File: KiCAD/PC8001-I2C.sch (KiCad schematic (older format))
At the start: 35 parts, among them J1 ADDR-JP, J2 I2C RTC DS3231, J3 I2C OUT, J4 PC8001 Ext Con, Q1 2N7000, U1 74HC138, U2 DS1307+, U3 8255, U4 74HC4066, U5 24LC1025, U6 24LC1025, Y1 32.768kHz

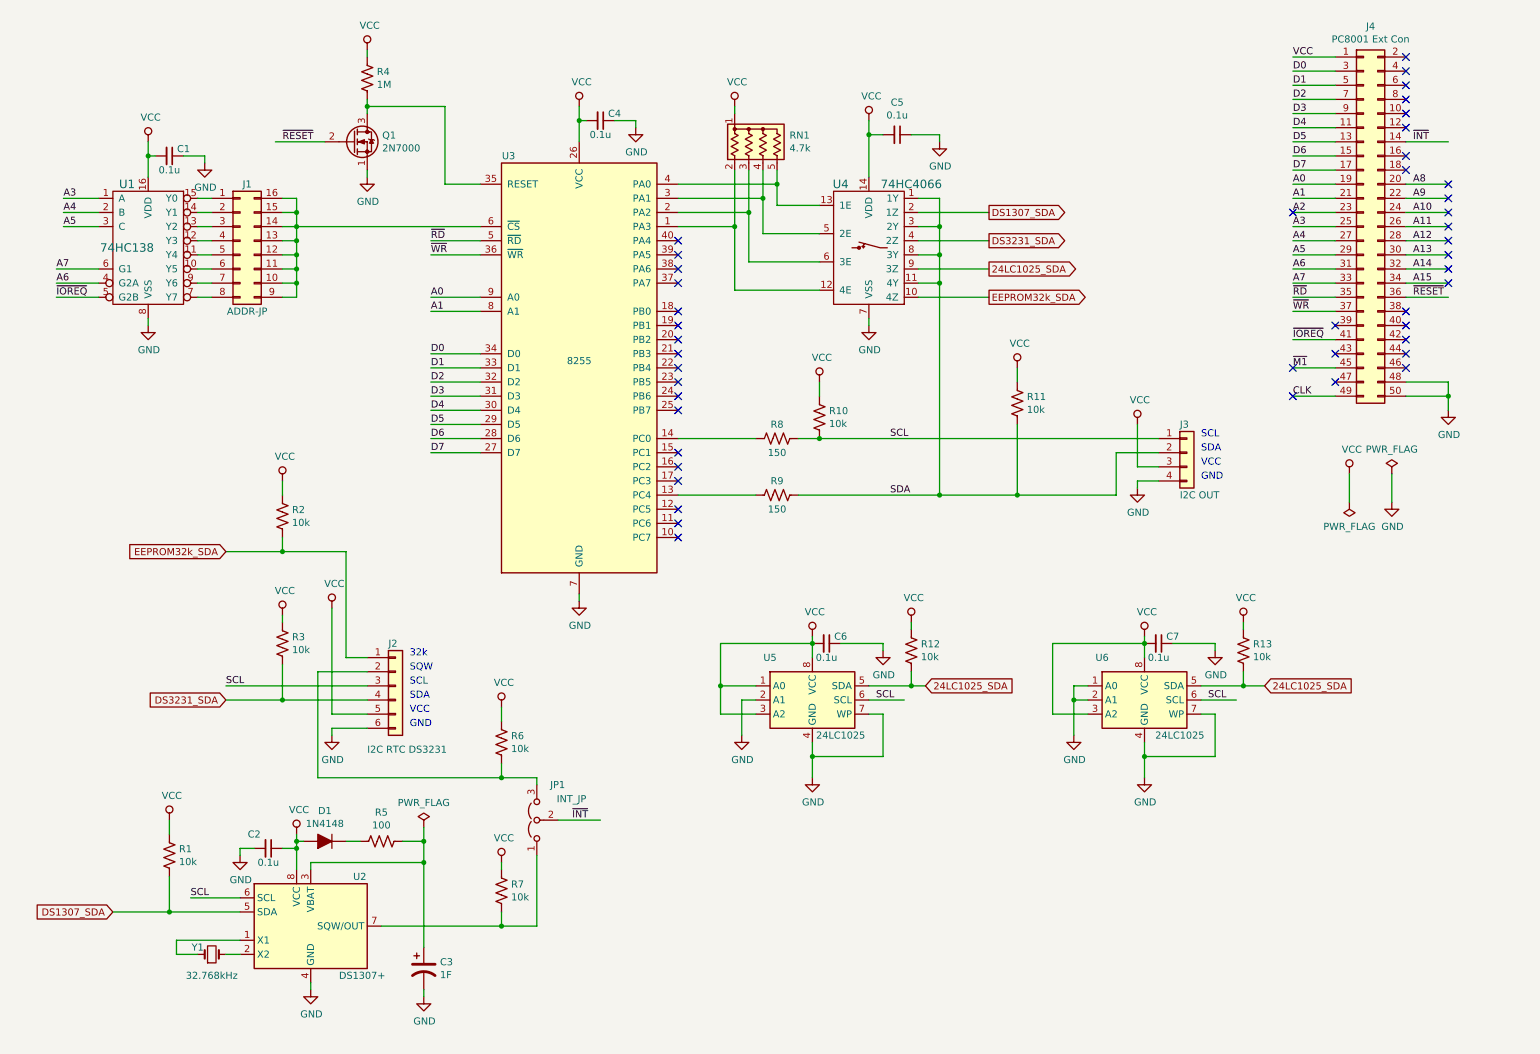
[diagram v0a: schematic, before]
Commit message: 回路変更、I2C RTC(DS3231)サンプル作成
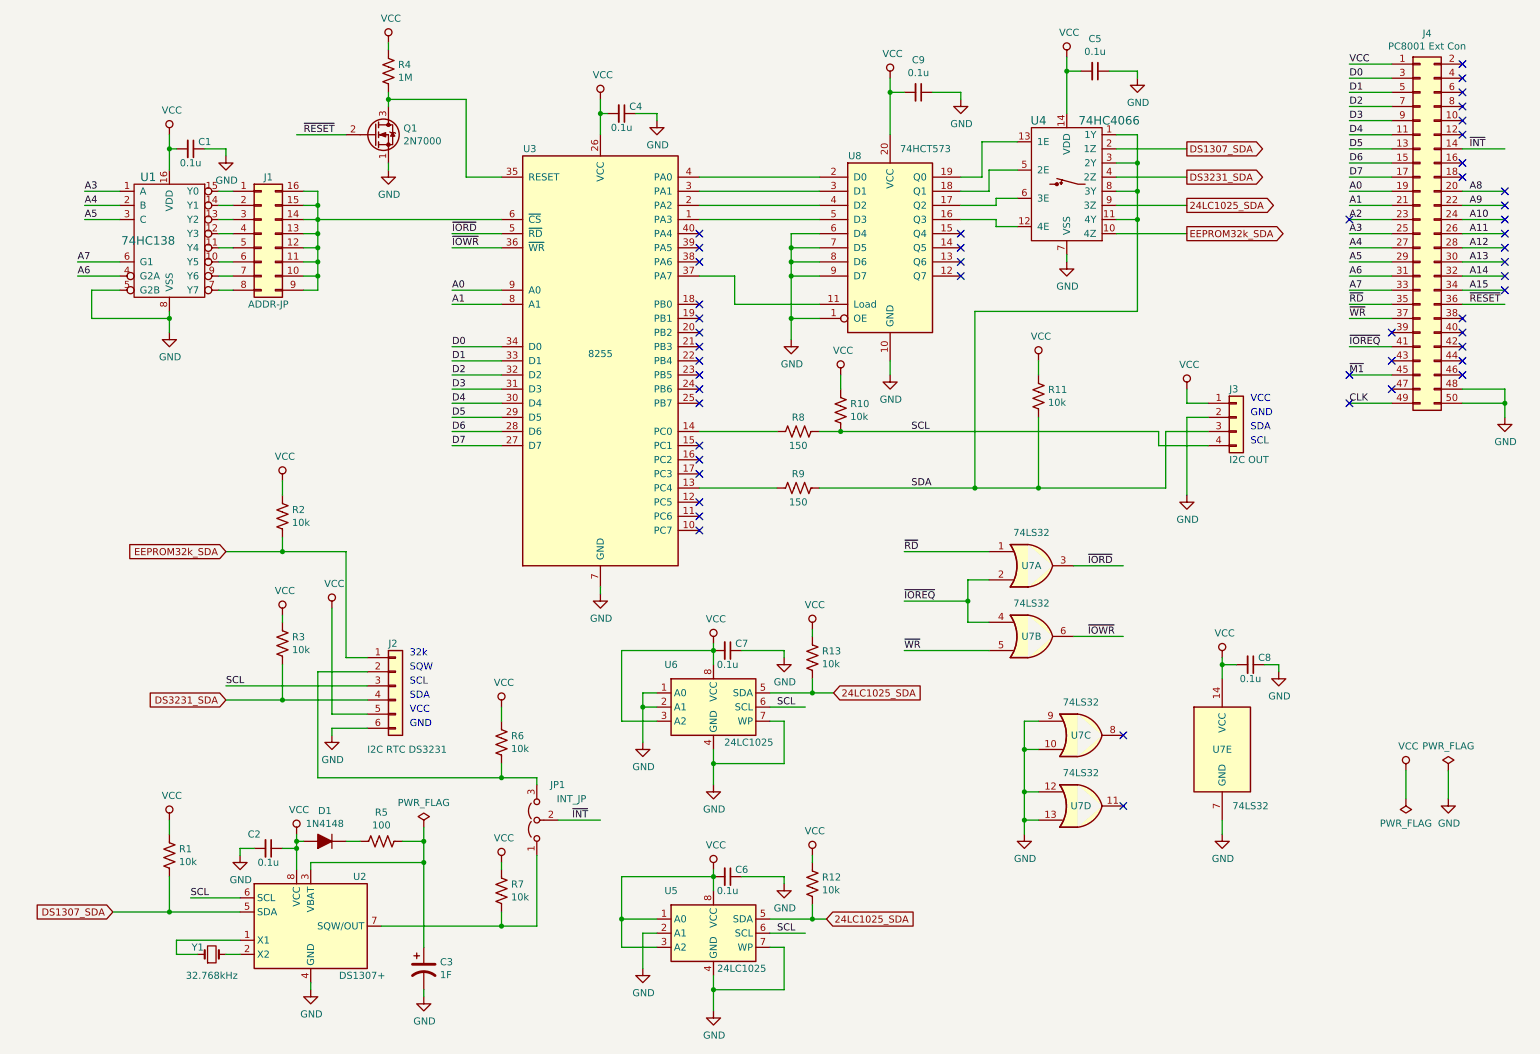
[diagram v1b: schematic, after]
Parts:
- removed RN1: 4.7k, Resistor_THT:R_Array_SIP5, symbol Device:R_Network04_US
- added C8, C9: 0.1u, symbol Device:C_Small
- added U7: 74LS32, symbol 74xx:74LS32
- added U8: 74HCT573, symbol 74xx:74LS573
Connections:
- net GND: now also J3.2 (Pin_2), U1.5 (G2B), C8.1, C9.1, U7.10, U7.12, U7.13, U7.7 (GND), U7.9, U8.1 (OE), U8.10 (GND), U8.6 (D4), U8.7 (D5), U8.8 (D6), U8.9 (D7); no longer J3.4 (Pin_4)
- net SCL: now also J3.4 (Pin_4); no longer J3.1 (Pin_1)
- net SDA: now also J3.3 (Pin_3); no longer J3.2 (Pin_2)
- net VCC: now also J3.1 (Pin_1), C8.2, C9.2, U7.14 (VCC), U8.20 (VCC); no longer J3.3 (Pin_3)
- net ~IOREQ: now also U7.2, U7.4; no longer U1.5 (G2B)
- net ~RD: now also U7.1; no longer U3.5 (~RD~)
- net ~WR: now also U7.5; no longer U3.36 (~WR~)
- net at U4.12 (4E): now also U8.16 (Q3); no longer U3.1 (PA3)
- net at U4.13 (1E): now also U8.19 (Q0); no longer U3.4 (PA0)
- net at U4.5 (2E): now also U8.18 (Q1); no longer U3.3 (PA1)
- net at U4.6 (3E): now also U8.17 (Q2); no longer U3.2 (PA2)
- net at U3.37 (PA7): now also U8.11 (Load)
- new net: U3.1 (PA3), U8.5 (D3)
- new net: U3.2 (PA2), U8.4 (D2)
- new net: U3.3 (PA1), U8.3 (D1)
- new net: U3.4 (PA0), U8.2 (D0)
- new net ~IORD: U3.5 (~RD~), U7.3
- new net ~IOWR: U3.36 (~WR~), U7.6
- no-connect marks 45 -> 50
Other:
- moved on the sheet: C1, C4, C5, C6, C7, J1, J3, J4, Q1, R10, R11, R12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

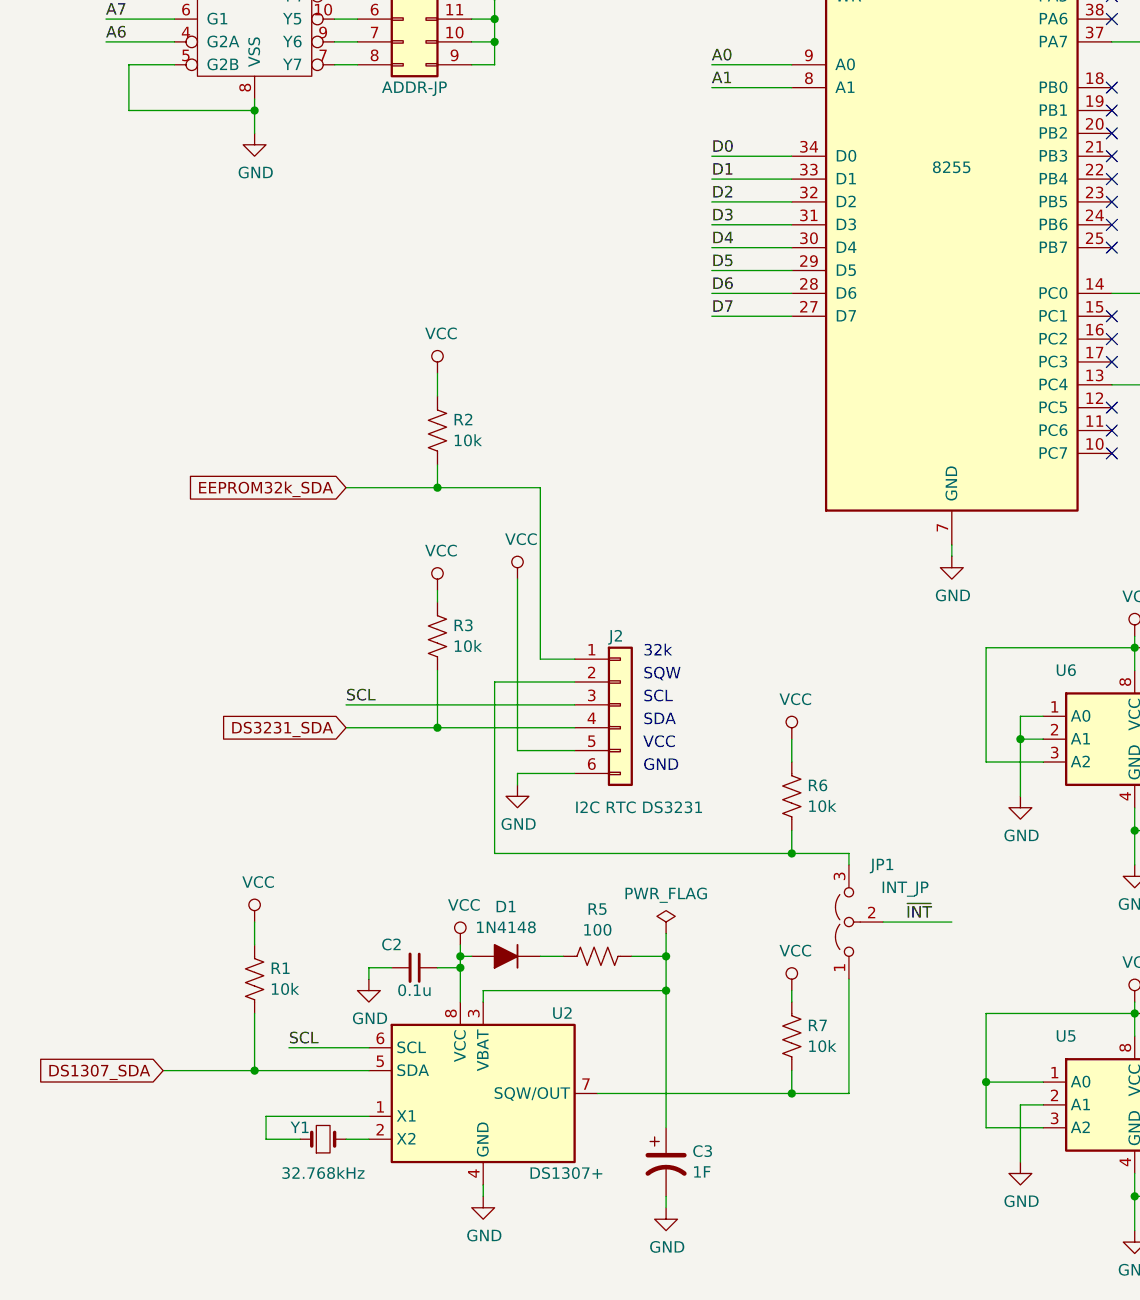
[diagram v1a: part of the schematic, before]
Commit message: サンブル機械語サブルーチンをBASICからCallする形で整備
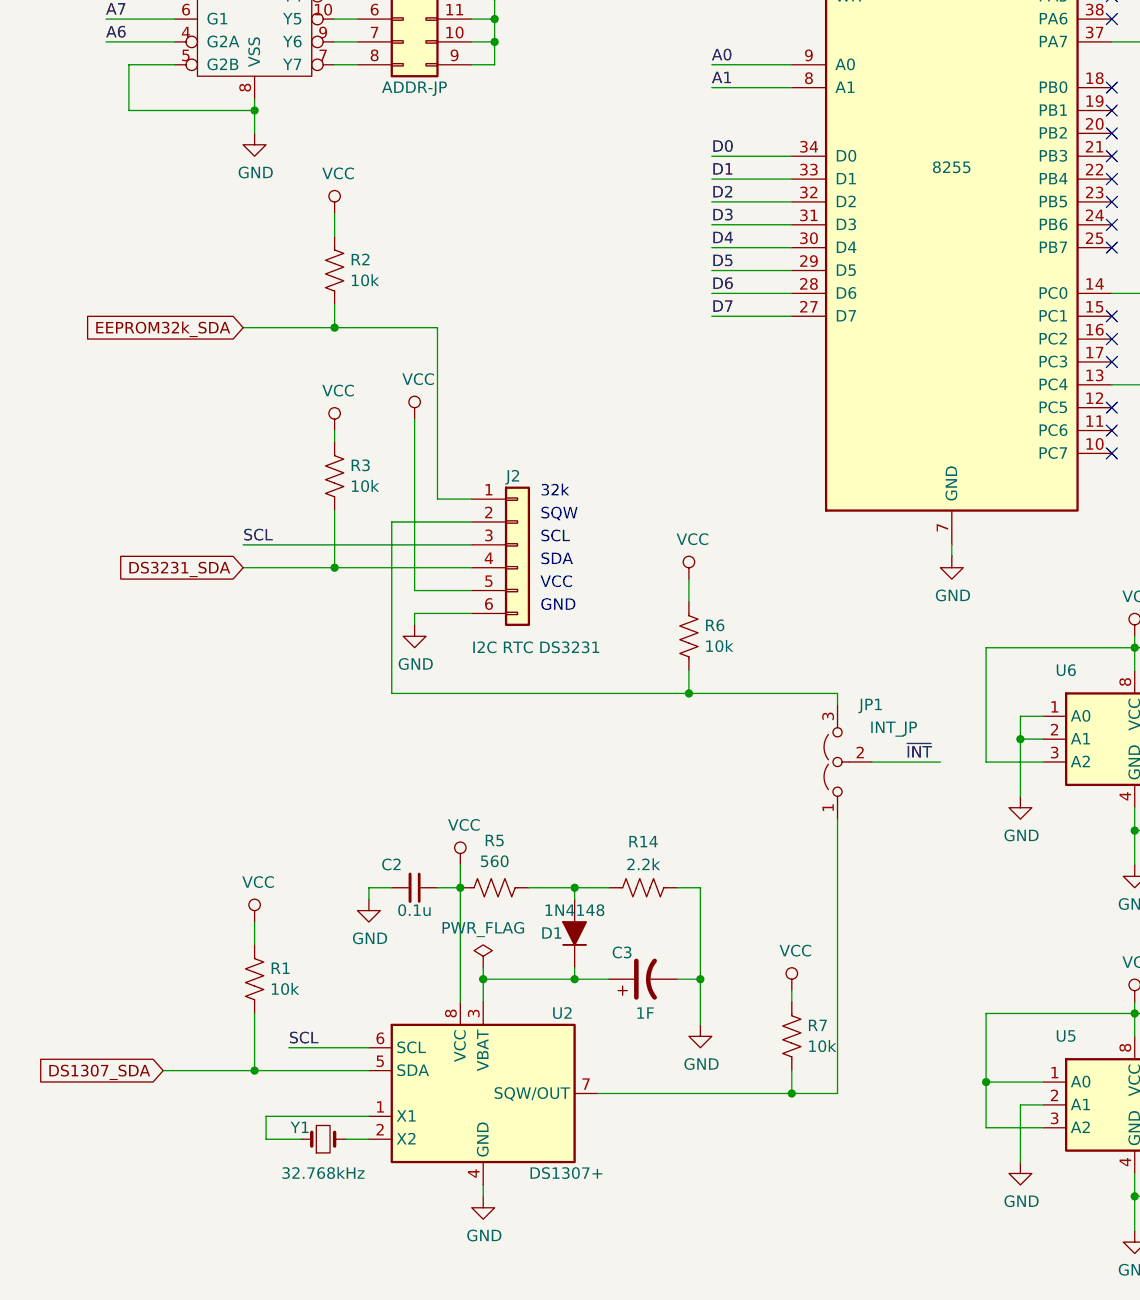
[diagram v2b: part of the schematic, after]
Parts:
- added R14: 2.2k, symbol Device:R_US
- R5: value 100 -> 560
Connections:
- net GND: now also R14.2
- net VCC: now also R5.2; no longer D1.2 (A)
- net at D1.1 (K): now also C3.1, U2.3 (VBAT); no longer R5.2
- new net: D1.2 (A), R14.1, R5.1
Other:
- moved on the sheet: C2, C3, D1, J2, JP1, R2, R3, R5, R6

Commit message: REV2 回路図検討
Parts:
- removed R10, R11: 10k, symbol Device:R_US
- removed U4: 74HC4066, symbol w_logic:74HC4066
- removed U8: 74HCT573, symbol 74xx:74LS573
- added J5, J6, J7, J8: I2C ExtOUT1, symbol Connector_Generic:Conn_01x04
- added RN1, RN2: 10k, Resistor_THT:R_Array_SIP5, symbol Device:R_Network04_US
- added U6: 74HC07, symbol 74xx:74LS07
- added U7: 74HC4051, symbol 74xx:74HC4051
- renumbered C7 to C5, C9 to C7, C5 to C9, R12 to R10, R8 to R11, R9 to R12, R5 to R4, R4 to R5, R14 to R6, R6 to R7, R7 to R8, R13 to R9, U6 to U4, U7 to U8
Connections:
- net 24LC1025_SDA: now also U7.5 (A5)
- net DS1307_SDA: now also U7.4 (A7)
- net DS3231_SDA: now also U7.2 (A6)
- net EEPROM32k_SDA: now also U7.1 (A4)
- net GND: now also J3.1 (Pin_1), J5.1 (Pin_1), J6.1 (Pin_1), J8.1 (Pin_1), U6.11, U6.13, U6.5, U6.7 (GND), U6.9, U7.6 (~E), U7.7 (VEE), U7.8 (GND); no longer J3.2 (Pin_2)
- net SCL: now also J5.4 (Pin_4), J6.4 (Pin_4), J7.4 (Pin_4), J8.4 (Pin_4), RN2.4 (R3)
- net SDA: now also RN2.5 (R4), U7.3 (A)
- net VCC: now also J3.2 (Pin_2), J5.2 (Pin_2), J6.2 (Pin_2), J7.2 (Pin_2), J8.2 (Pin_2), RN1.1 (common), RN2.1 (common), U6.14 (VCC), U7.16 (VCC); no longer J3.1 (Pin_1)
- net at R11.1: now also U3.13 (PC4), U6.2; no longer U3.14 (PC0)
- net at U3.12 (PC5): now also R12.1, U6.4
- net at U3.15 (PC1): now also RN2.3 (R2), U6.3
- net at U3.2 (PA2): now also RN1.4 (R3), U7.9 (S2)
- net at U3.3 (PA1): now also RN1.3 (R2), U7.10 (S1)
- net at U3.4 (PA0): now also RN1.2 (R1), U7.11 (S0)
- new net: RN2.2 (R1), U3.14 (PC0), U6.1
- new net ExtSDA-1: J5.3 (Pin_3), U7.13 (A0)
- new net ExtSDA-2: J6.3 (Pin_3), U7.14 (A1)
- new net ExtSDA-3: J7.3 (Pin_3), U7.15 (A2)
- new net ExtSDA-4: J8.3 (Pin_3), U7.12 (A3)
- no-connect marks 50 -> 51
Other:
- moved on the sheet: C7, C8, C9, R11, R12, U8C, U8D, U8E
